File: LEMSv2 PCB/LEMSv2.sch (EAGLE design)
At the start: 83 parts, among them J2 M05, Q1 200mA/50V, Q10 200mA/50V, Q2 200mA/50V, Q3 200mA/50V, Q4 200mA/50V, Q5 200mA/50V, Q6 200mA/50V, Q7 200mA/50V, Q8 MMBT3904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

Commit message: Modified SD connector footprint, moved connectors
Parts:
- U1: value SDMMC06132 -> (none)

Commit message: Initial layout
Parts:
- C2, C3, C4, C5, C6, C7, C8: device LEMSv2:CAP0805 -> LEMSv2:CAP
- J1: value (none) -> FEMALE 2x3; device LEMSv2:M03X2FEMALE_SMD -> LEMSv2:M03X2FEMALE
- J2: value M05 -> (none); device LEMSv2:M05 -> SparkFun-Connectors:M05PTH
- J3: device LEMSv2:M06SMD-STRAIGHT-COMBO-FEMALE -> LEMSv2:M06SILK_FEMALE_PTH
- J4, J5: device LEMSv2:M08SMD-COMBO-FEMALE -> LEMSv2:M08
- J6: device LEMSv2:M10SMD_COMBO-FEMALE -> LEMSv2:M10SILK_FEMALE_PTH
- renumbered D1 to LED1, D2 to LED2
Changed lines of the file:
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@@
 <part name="GND3" library="LEMSv2" deviceset="GND" device=""/>
 <part name="PS1" library="LEMSv2" deviceset="TSR_1-2450" device=""/>
-<part name="J1" library="LEMSv2" deviceset="M03X2" device="FEMALE_SMD"/>
-<part name="J3" library="LEMSv2" deviceset="M06" device="SMD-STRAIGHT-COMBO-FEMALE"/>
-<part name="J4" library="LEMSv2" deviceset="M08" device="SMD-COMBO-FEMALE"/>
-<part name="J5" library="LEMSv2" deviceset="M08" device="SMD-COMBO-FEMALE"/>
-<part name="J2" library="LEMSv2" deviceset="M05" device=""/>
-<part name="J6" library="LEMSv2" deviceset="M10" device="SMD_COMBO-FEMALE"/>
+<part name="J1" library="LEMSv2" deviceset="M03X2" device="FEMALE" value="FEMALE 2x3"/>
+<part name="J3" library="LEMSv2" deviceset="M06" device="SILK_FEMALE_PTH"/>
+<part name="J4" library="LEMSv2" deviceset="M08" device=""/>
+<part name="J5" library="LEMSv2" deviceset="M08" device=""/>
+<part name="J2" library="SparkFun-Connectors" deviceset="M05" device="PTH"/>
+<part name="J6" library="LEMSv2" deviceset="M10" device="SILK_FEMALE_PTH"/>
 <part name="C1" library="LEMSv2" deviceset="CAP_POL" device="PTH2" value="22uF"/>
 <part name="SUPPLY2" library="SparkFun-Aesthetics" deviceset="5V" device=""/>
-<part name="C2" library="LEMSv2" deviceset="CAP" device="0805"/>
+<part name="C2" library="LEMSv2" deviceset="CAP" device=""/>
 <part name="GND1" library="LEMSv2" deviceset="GND" device=""/>
 <part name="SUPPLY3" library="LEMSv2" deviceset="3.3V" device=""/>
@@
 <part name="U$3" library="LEMSv2" deviceset="MOUNTINGHOLE" device="2.5"/>
 <part name="U$4" library="LEMSv2" deviceset="MOUNTINGHOLE" device="2.5"/>
-<part name="C3" library="LEMSv2" deviceset="CAP" device="0805" value="0.1uF"/>
+<part name="C3" library="LEMSv2" deviceset="CAP" device="" value="0.1uF"/>
 <part name="U3" library="LEMSv2" deviceset="TLV2372" device=""/>
 <part name="SUPPLY10" library="LEMSv2" deviceset="5V" device=""/>
@@
 <part name="J13" library="LEMSv2" deviceset="M03" device="PTH"/>
 <part name="GND6" library="LEMSv2" deviceset="GND" device=""/>
-<part name="C4" library="LEMSv2" deviceset="CAP" device="0805" value="1uF"/>
+<part name="C4" library="LEMSv2" deviceset="CAP" device="" value="1uF"/>
 <part name="R14" library="adafruit" deviceset="R-US_" device="FLIPFLOP"/>
 <part name="U4" library="LEMSv2" deviceset="BMP280" device=""/>
-<part name="C5" library="LEMSv2" deviceset="CAP" device="0805"/>
-<part name="C6" library="LEMSv2" deviceset="CAP" device="0805"/>
+<part name="C5" library="LEMSv2" deviceset="CAP" device=""/>
+<part name="C6" library="LEMSv2" deviceset="CAP" device=""/>
 <part name="GND7" library="LEMSv2" deviceset="GND" device=""/>
 <part name="Q8" library="LEMSv2" deviceset="MMBT3904" device=""/>
@@
 <part name="R17" library="LEMSv2" deviceset="RESISTOR" device="_0805" value="1k"/>
 <part name="R18" library="LEMSv2" deviceset="RESISTOR" device="_0805" value="1k"/>
-<part name="D1" library="LEMSv2" deviceset="LED_GREEN" device="" value="GREEN"/>
-<part name="D2" library="LEMSv2" deviceset="LED_RED" device="" value="RED"/>
+<part name="LED1" library="LEMSv2" deviceset="LED_GREEN" device="" value="GREEN"/>
+<part name="LED2" library="LEMSv2" deviceset="LED_RED" device="" value="RED"/>
 <part name="SUPPLY11" library="LEMSv2" deviceset="3.3V" device=""/>
 <part name="SUPPLY12" library="LEMSv2" deviceset="3.3V" device=""/>
 <part name="FB1" library="LEMSv2" deviceset="FERRITE" device=""/>
 <part name="U5" library="LEMSv2" deviceset="ADC_ADS1115" device=""/>
-<part name="C7" library="LEMSv2" deviceset="CAP" device="0805" value="1uF"/>
-<part name="C8" library="LEMSv2" deviceset="CAP" device="0805" value="1nF"/>
+<part name="C7" library="LEMSv2" deviceset="CAP" device="" value="1uF"/>
+<part name="C8" library="LEMSv2" deviceset="CAP" device="" value="1nF"/>
 <part name="SUPPLY13" library="LEMSv2" deviceset="5V" device=""/>
 <part name="GND10" library="LEMSv2" deviceset="GND" device=""/>
@@
 <instance part="R17" gate="G$1" x="10.16" y="114.3"/>
 <instance part="R18" gate="G$1" x="45.72" y="114.3"/>
-<instance part="D1" gate="G$1" x="20.32" y="124.46"/>
-<instance part="D2" gate="G$1" x="55.88" y="124.46"/>
+<instance part="LED1" gate="G$1" x="20.32" y="124.46"/>
+<instance part="LED2" gate="G$1" x="55.88" y="124.46"/>
 <instance part="SUPPLY11" gate="G$1" x="20.32" y="137.16"/>
 <instance part="SUPPLY12" gate="G$1" x="55.88" y="137.16"/>
@@
 <segment>
 <pinref part="Q8" gate="G$1" pin="C"/>
-<pinref part="D1" gate="G$1" pin="C"/>
+<pinref part="LED1" gate="G$1" pin="C"/>
 </segment>
 </net>
@@
 <segment>
 <pinref part="Q9" gate="G$1" pin="C"/>
-<pinref part="D2" gate="G$1" pin="C"/>
+<pinref part="LED2" gate="G$1" pin="C"/>
 </segment>
 </net>
 <net name="N$9" class="0">
 <segment>
-<pinref part="D1" gate="G$1" pin="A"/>
+<pinref part="LED1" gate="G$1" pin="A"/>
 <pinref part="R15" gate="G$1" pin="1"/>
 </segment>
@@
 <net name="N$10" class="0">
 <segment>
-<pinref part="D2" gate="G$1" pin="A"/>
+<pinref part="LED2" gate="G$1" pin="A"/>
 <pinref part="R16" gate="G$1" pin="1"/>
 </segment>

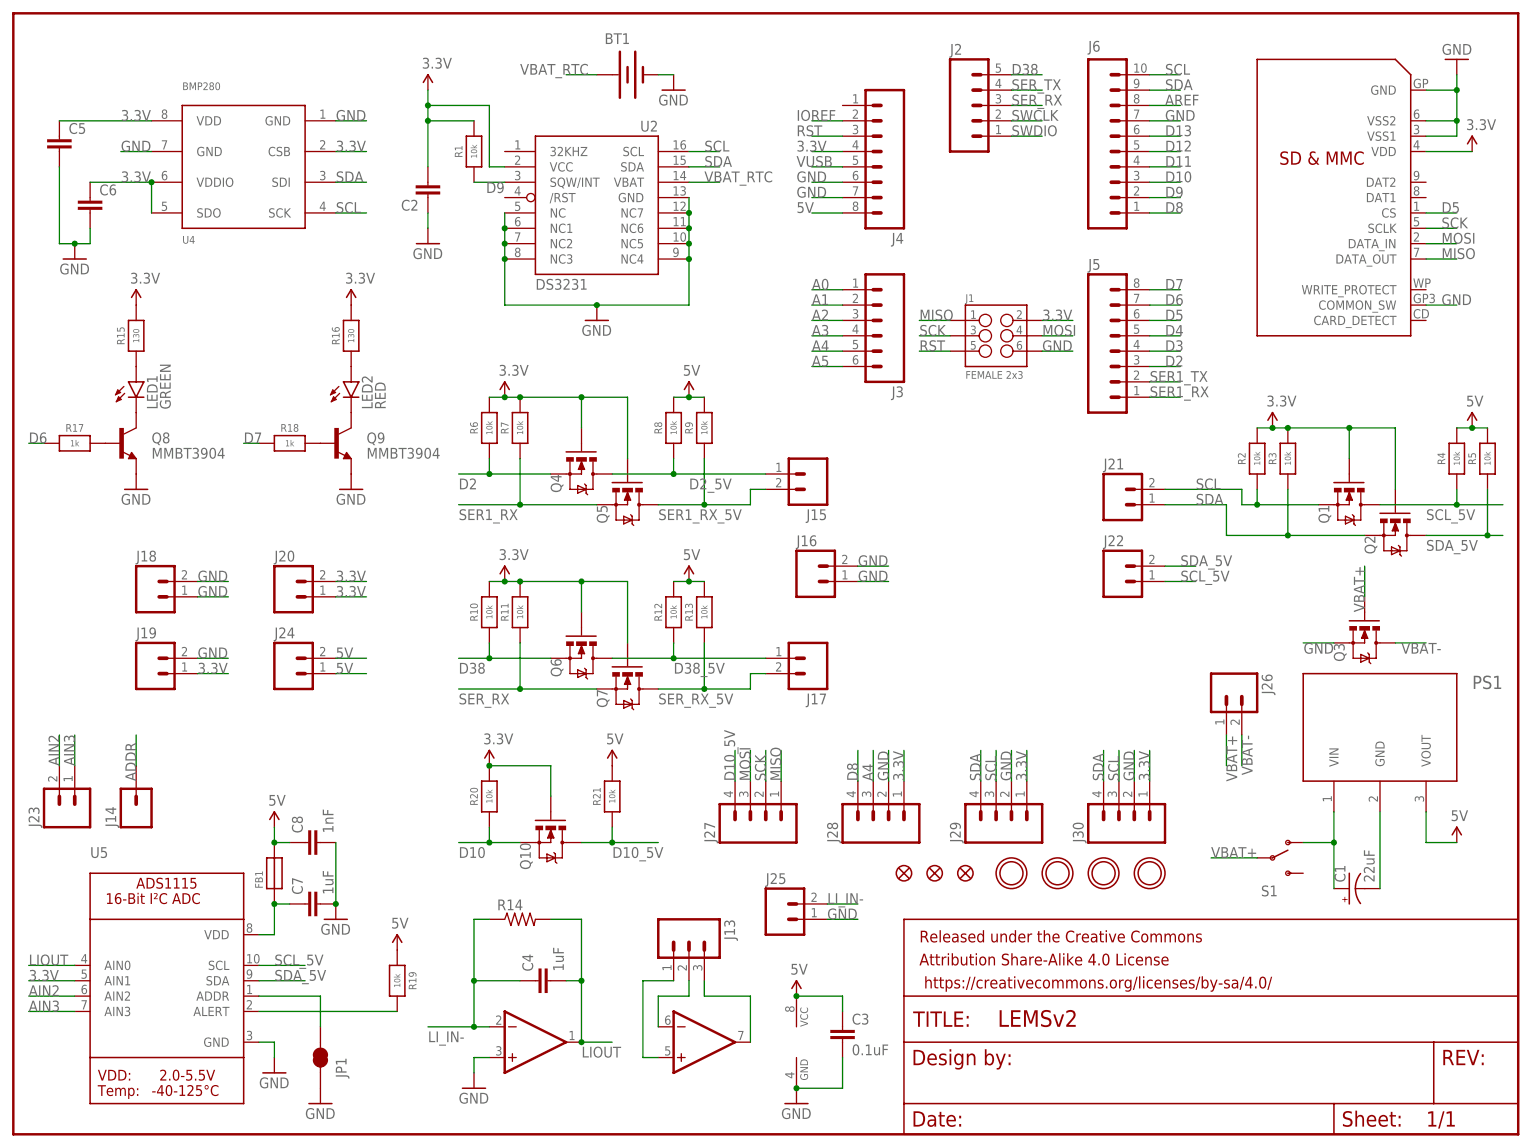
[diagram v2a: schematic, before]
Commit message: 5TM library bug fix, board layout changes
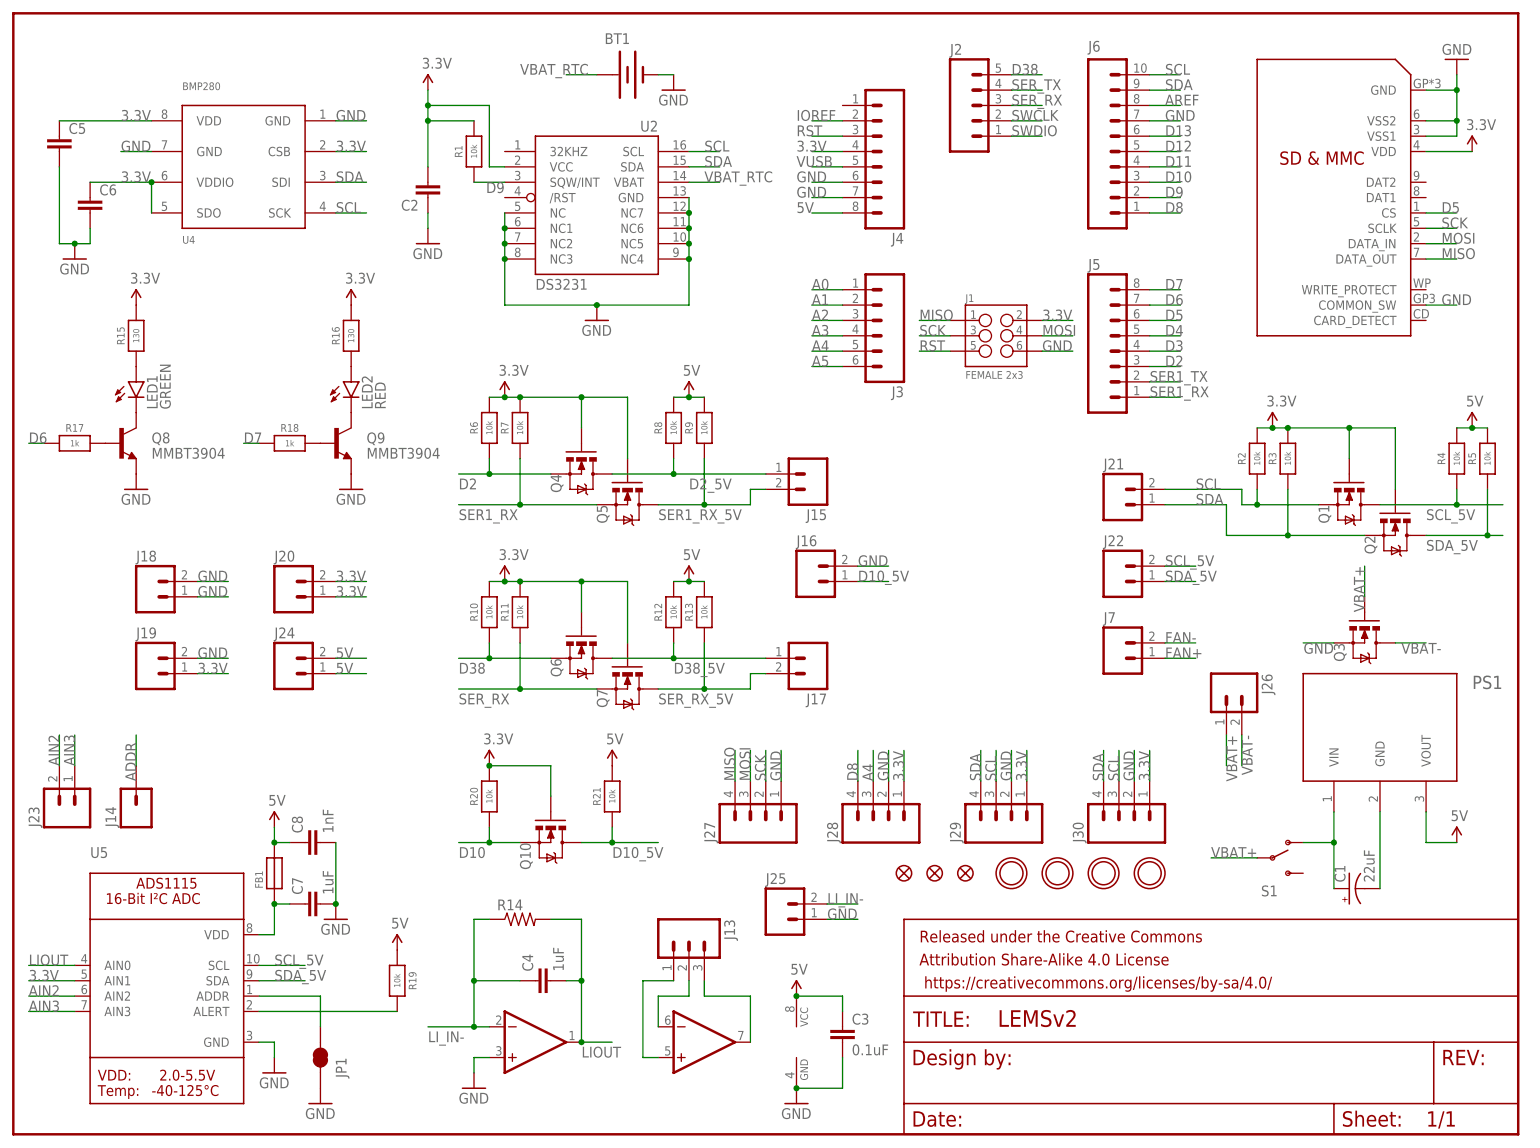
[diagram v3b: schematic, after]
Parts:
- added J7: (no value), LEMSv2:M023.5MM
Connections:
- new net FAN+: J7.1
- new net FAN-: J7.2
- net D10_5V: now also J16.1; no longer J27.4
- net GND: now also J27.1; no longer J16.1
- net MISO: now also J27.4; no longer J27.1
- net SCL_5V: now also J22.2; no longer J22.1
- net SDA_5V: now also J22.1; no longer J22.2
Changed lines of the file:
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@@
 <part name="SUPPLY16" library="SparkFun-Aesthetics" deviceset="5V" device=""/>
 <part name="Q10" library="LEMSv2" deviceset="MOSFET-NCHANNEL" device="BSS138" value="200mA/50V"/>
+<part name="J7" library="LEMSv2" deviceset="M02" device="3.5MM"/>
 </parts>
 <sheets>
@@
 <attribute name="NAME" x="83.82" y="48.26" size="1.778" layer="95" rot="R270"/>
 </instance>
+<instance part="J7" gate="G$1" x="182.88" y="78.74"/>
 </instances>
 <busses>
@@
 </segment>
 <segment>
-<pinref part="J16" gate="G$1" pin="1"/>
-<wire x1="139.7" y1="91.44" x2="144.78" y2="91.44" width="0.1524" layer="91"/>
-<label x="139.7" y="91.44" size="1.778" layer="95"/>
-</segment>
-<segment>
 <pinref part="J18" gate="G$1" pin="2"/>
 <wire x1="30.48" y1="91.44" x2="35.56" y2="91.44" width="0.1524" layer="91"/>
@@
 <label x="134.62" y="35.56" size="1.778" layer="95"/>
 </segment>
+<segment>
+<pinref part="J27" gate="G$1" pin="1"/>
+<wire x1="127" y1="58.42" x2="127" y2="63.5" width="0.1524" layer="91"/>
+<label x="127" y="58.42" size="1.778" layer="95" rot="R90"/>
+</segment>
 </net>
 <net name="SCK" class="0">
@@
 </segment>
 <segment>
-<pinref part="J27" gate="G$1" pin="1"/>
-<wire x1="127" y1="58.42" x2="127" y2="63.5" width="0.1524" layer="91"/>
-<label x="127" y="58.42" size="1.778" layer="95" rot="R90"/>
+<pinref part="J27" gate="G$1" pin="4"/>
+<wire x1="119.38" y1="58.42" x2="119.38" y2="63.5" width="0.1524" layer="91"/>
+<label x="119.38" y="58.42" size="1.778" layer="95" rot="R90"/>
 </segment>
 </net>
@@
 </segment>
 <segment>
-<pinref part="J22" gate="G$1" pin="1"/>
-<wire x1="190.5" y1="91.44" x2="195.58" y2="91.44" width="0.1524" layer="91"/>
-<label x="193.04" y="91.44" size="1.778" layer="95"/>
+<pinref part="J22" gate="G$1" pin="2"/>
+<wire x1="190.5" y1="93.98" x2="195.58" y2="93.98" width="0.1524" layer="91"/>
+<label x="190.5" y="93.98" size="1.778" layer="95"/>
 </segment>
 </net>
@@
 </segment>
 <segment>
-<pinref part="J22" gate="G$1" pin="2"/>
-<wire x1="190.5" y1="93.98" x2="195.58" y2="93.98" width="0.1524" layer="91"/>
-<label x="193.04" y="93.98" size="1.778" layer="95"/>
+<pinref part="J22" gate="G$1" pin="1"/>
+<wire x1="190.5" y1="91.44" x2="195.58" y2="91.44" width="0.1524" layer="91"/>
+<label x="190.5" y="91.44" size="1.778" layer="95"/>
 </segment>
 </net>
@@
 </segment>
 <segment>
-<pinref part="J27" gate="G$1" pin="4"/>
-<wire x1="119.38" y1="58.42" x2="119.38" y2="63.5" width="0.1524" layer="91"/>
-<label x="119.38" y="58.42" size="1.778" layer="95" rot="R90"/>
-</segment>
-</net>
+<pinref part="J16" gate="G$1" pin="1"/>
+<wire x1="139.7" y1="91.44" x2="144.78" y2="91.44" width="0.1524" layer="91"/>
+<label x="139.7" y="91.44" size="1.778" layer="95"/>
+</segment>
+</net>
+<net name="FAN-" class="0">
+<segment>
+<pinref part="J7" gate="G$1" pin="2"/>
+<wire x1="190.5" y1="81.28" x2="195.58" y2="81.28" width="0.1524" layer="91"/>
+<label x="190.5" y="81.28" size="1.778" layer="95"/>
+</segment>
+</net>
+<net name="FAN+" class="0">
+<segment>
+<pinref part="J7" gate="G$1" pin="1"/>
+<wire x1="190.5" y1="78.74" x2="195.58" y2="78.74" width="0.1524" layer="91"/>
+<label x="190.5" y="78.74" size="1.778" layer="95"/>
+</segment>
+</net>

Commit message: Switched 5TM power to transistor, added schottky
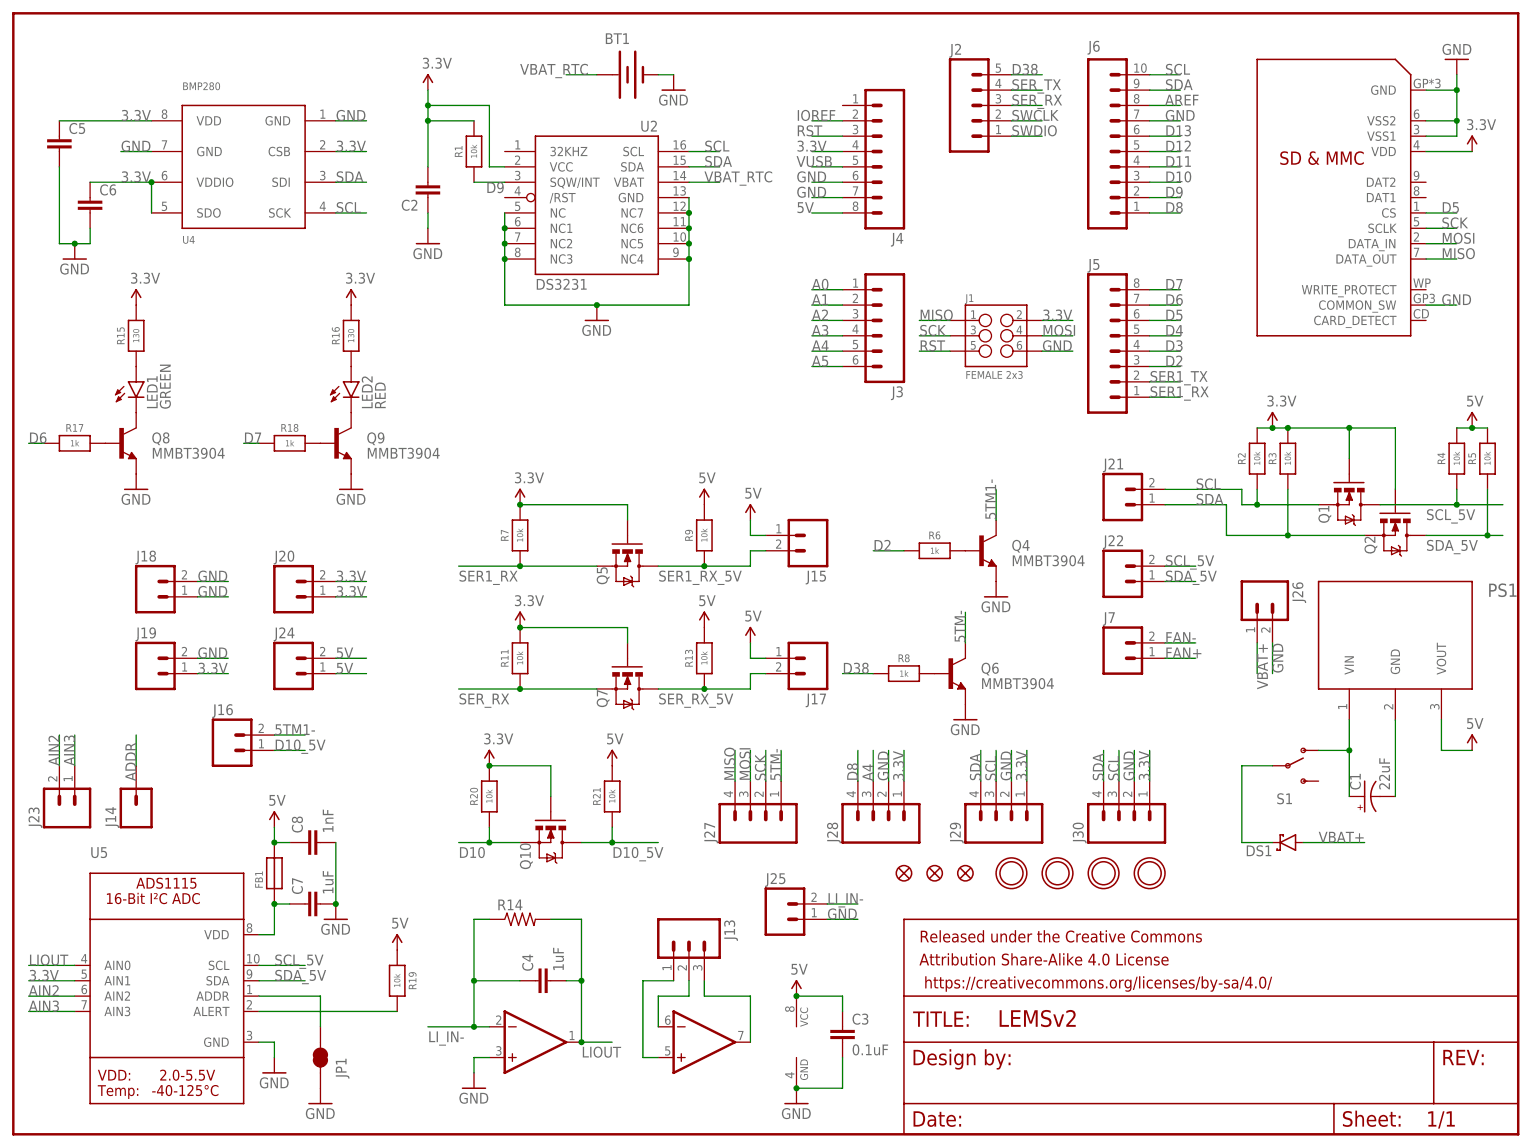
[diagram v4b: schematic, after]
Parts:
- removed Q3: 200mA/50V, LEMSv2:MOSFET-NCHANNELBSS138
- removed R10, R12: 10k, LEMSv2:RESISTOR_0805
- added DS1: DIODE_SCHOTTKY, LEMSv2:DIODE_SCHOTTKY
- Q4, Q6: value 200mA/50V -> MMBT3904; device LEMSv2:MOSFET-NCHANNELBSS138 -> LEMSv2:MMBT3904
- R6, R8: value 10k -> 1k
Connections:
- removed net D2_5V: J15.1, Q4.D, R8.1
- removed net D38_5V: J17.1, Q6.D, R12.1
- removed net VBAT-: J26.2, Q3.D
- new net 5TM-: J27.1, Q6.C
- new net 5TM1-: J16.2, Q4.C
- new net N$11: Q4.B, R6.2
- new net N$12: Q6.B, R8.2
- new net N$13: DS1.C, S1.P
- net 3.3V: no longer Q4.G, Q6.G, R10.2, R6.2
- net 5V: now also J15.1, J17.1; no longer R12.2, R8.2
- net D2: no longer Q4.S
- net D38: now also R8.1; no longer Q6.S, R10.1
- net GND: now also J26.2, Q4.E, Q6.E; no longer J16.2, J27.1, Q3.S
- net VBAT+: now also DS1.A; no longer Q3.G, S1.P
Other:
- moved on the sheet: C1, J15, J16, J26, PS1, Q5, R11, R13, R6, R7, R8, R9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
